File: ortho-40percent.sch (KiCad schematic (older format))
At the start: 7 parts

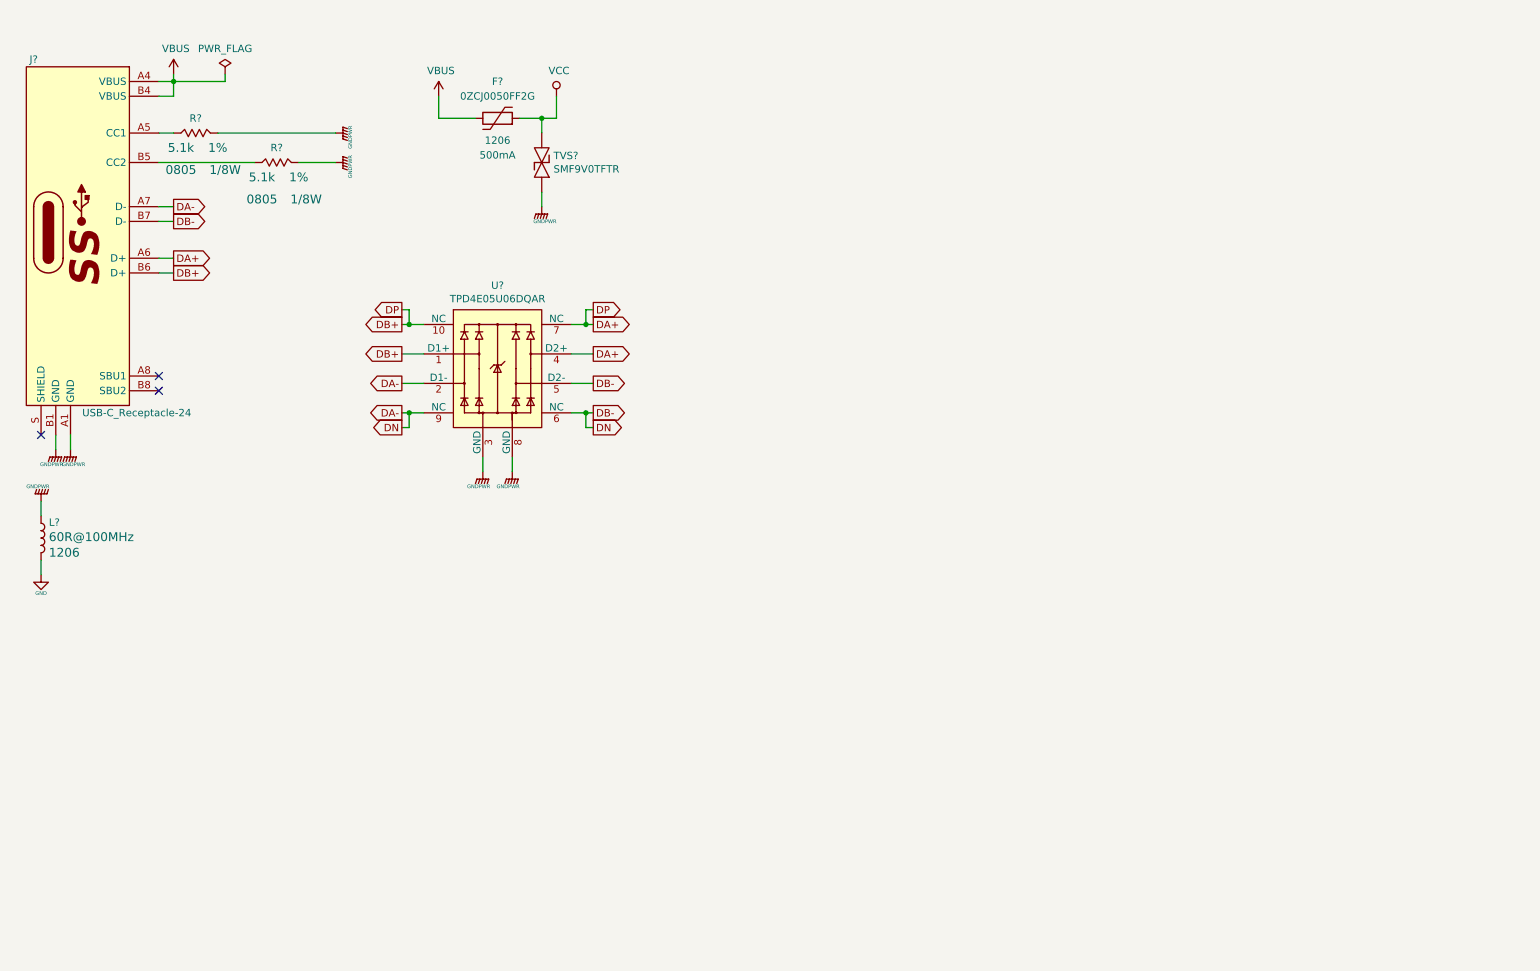
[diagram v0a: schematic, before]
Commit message: Created KeyMatrix schematic
Added new footprints and associated 3d models. Created KeyMatrix schematic sheet.
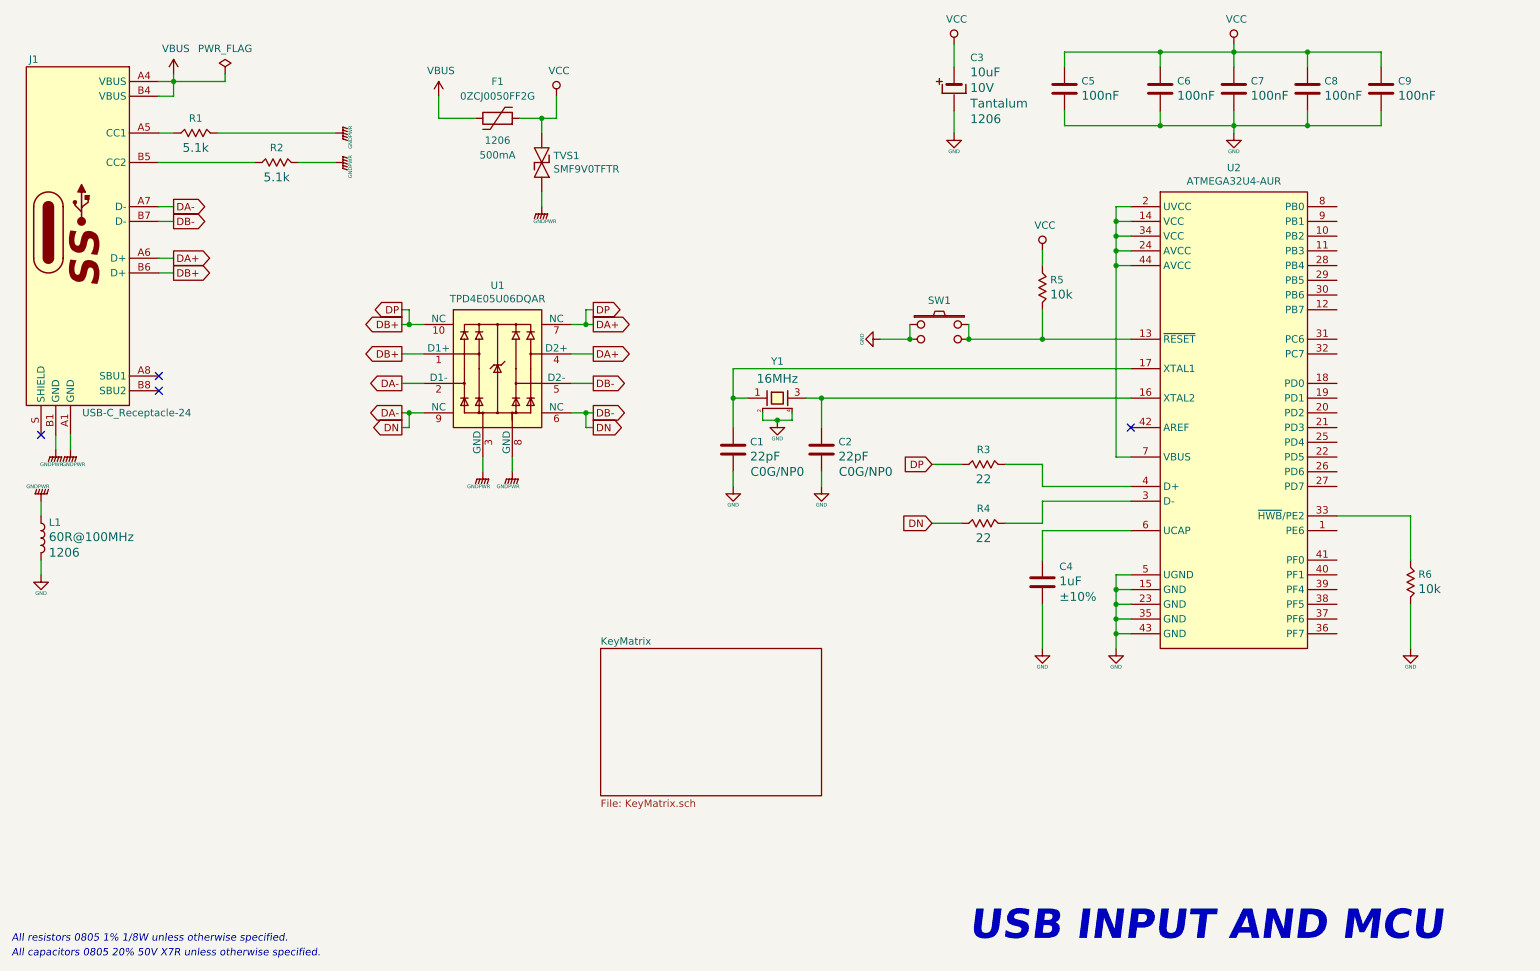
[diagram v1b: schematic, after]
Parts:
- added C1, C2, C4, C5, C6, C7, C8, C9: C, ortho-40percent:C_0805, symbol master-vampire_General:C
- added C3: CP_tantalum, ortho-40percent:CP_TANTALUM_1206, symbol master-vampire_General:CP_tantalum
- added R3, R4, R5, R6: R, ortho-40percent:R_0805, symbol master-vampire_General:R
- added SW1: SW_NO_4-Pin, ortho-40percent:SW_C+K_4-SMD-Gullwing_5.2x5.2mm_H1.6mm, symbol master-vampire_General:SW_NO_4-Pin
- added U2: U_ATmega32u4-AU, ortho-40percent:TQFP-44, symbol master-vampire_General:U_ATmega32u4-AU
- added Y1: XTAL_4Lead, ortho-40percent:XTAL_4-SMD_3.2x2.5mm, symbol master-vampire_General:XTAL_4Lead
- R1, R2: renamed from R?; footprint (none) -> ortho-40percent:R_0805
- TVS1: renamed from TVS?; footprint ortho-40percent:D_SOD-123F -> ortho-40percent:SOD-123F
- gave numbers to parts that had none: 4
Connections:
- net DA+: now also R3.2
- net DA-: now also R4.2
- net GND: now also C1.2, C2.2, C3.2, C4.2, C5.2, C6.2, C7.2, C8.2, C9.2, R6.1, SW1.1 (in), SW1.2 (in), U2.15 (GND), U2.23 (GND), U2.35 (GND), U2.43 (GND), U2.5 (UGND), Y1.2 (case), Y1.4 (case)
- net VCC: now also C3.1, C5.1, C6.1, C7.1, C8.1, C9.1, R5.2
- new net: C1.1, U2.17 (XTAL1), Y1.1
- new net: R5.1, SW1.3 (out), SW1.4 (out), U2.13 (~RESET)
- new net: U2.14 (VCC), U2.2 (UVCC), U2.24 (AVCC), U2.34 (VCC), U2.44 (AVCC), U2.7 (VBUS)
- new net: C2.1, U2.16 (XTAL2), Y1.3
- new net: R4.1, U2.3 (D-)
- new net: R6.2, U2.33 (~HWB~/PE2)
- new net: R3.1, U2.4 (D+)
- new net: C4.1, U2.6 (UCAP)
- no-connect marks 3 -> 4
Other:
- note added: "All capacitors 0805 20% 50V X7R unless otherwise specified."
- note added: "All resistors 0805 1% 1/8W unless otherwise specified."
- note added: "USB INPUT AND MCU"

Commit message: Case outline and mounting
Received kprepublic case, used dimensions to set drawing of case and pcb outline. Created M2 screw footprint and added mounting holes to project. Tied screws to power gnd, will possibly change to signal ground later. Changed switches to be kailh hotswaps.
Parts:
- added H1, H2, H3, H4, H5: H_MountingHole_Screw_withPin, ortho-40percent:H_Screw-M2_Countersunk, symbol master-vampire_General:H_MountingHole_Screw_withPin
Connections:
- net GNDPWR: now also H1.1, H2.1, H3.1, H4.1, H5.1
- net VCC: now also U2.14 (VCC), U2.2 (UVCC), U2.24 (AVCC), U2.34 (VCC), U2.44 (AVCC), U2.7 (VBUS)
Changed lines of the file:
@@
 F1 "KeyMatrix.sch" 50
 $EndSheet
+$Comp
+L power:VCC #PWR026
+U 1 1 604393E0
+P 8500 1850
+F 0 "#PWR026" H 8500 1700 50  0001 C CNN
+F 1 "VCC" H 8517 2023 50  0000 C CNN
+F 2 "" H 8500 1850 50  0001 C CNN
+F 3 "" H 8500 1850 50  0001 C CNN
+	1    8500 1850
+	1    0    0    -1
+$EndComp
+Wire Wire Line
+	8500 1850 8500 2000
+Connection ~ 8500 2000
+$Comp
+L master-vampire_General:H_MountingHole_Screw_withPin H1
+U 1 1 604407EC
+P 1500 5100
+F 0 "H1" V 1650 5050 50  0000 L CNN
+F 1 "H_MountingHole_Screw_withPin" H 1628 5055 50  0001 L CNN
+F 2 "ortho-40percent:H_Screw-M2_Countersunk" H 1500 5100 50  0001 C CNN
+F 3 "" H 1500 5100 50  0001 C CNN
+F 4 "DNP" H 1600 5300 50  0001 C CNN "MPN"
+F 5 "DNP" H 1700 5400 50  0001 C CNN "Manufacturer"
+F 6 "DNP" H 1800 5500 50  0001 C CNN "Supplier PN"
+F 7 "DNP" H 1900 5600 50  0001 C CNN "Supplier"
+F 8 "DNP" H 2000 5700 50  0001 C CNN "Package"
+	1    1500 5100
+	0    -1   -1   0
+$EndComp
+$Comp
+L master-vampire_General:H_MountingHole_Screw_withPin H2
+U 1 1 6041FFC7
+P 1750 5100
+F 0 "H2" V 1900 5050 50  0000 L CNN
+F 1 "H_MountingHole_Screw_withPin" H 1878 5055 50  0001 L CNN
+F 2 "ortho-40percent:H_Screw-M2_Countersunk" H 1750 5100 50  0001 C CNN
+F 3 "" H 1750 5100 50  0001 C CNN
+F 4 "DNP" H 1850 5300 50  0001 C CNN "MPN"
+F 5 "DNP" H 1950 5400 50  0001 C CNN "Manufacturer"
+F 6 "DNP" H 2050 5500 50  0001 C CNN "Supplier PN"
+F 7 "DNP" H 2150 5600 50  0001 C CNN "Supplier"
+F 8 "DNP" H 2250 5700 50  0001 C CNN "Package"
+	1    1750 5100
+	0    -1   -1   0
+$EndComp
+$Comp
+L master-vampire_General:H_MountingHole_Screw_withPin H3
+U 1 1 60420244
+P 2000 5100
+F 0 "H3" V 2150 5050 50  0000 L CNN
+F 1 "H_MountingHole_Screw_withPin" H 2128 5055 50  0001 L CNN
+F 2 "ortho-40percent:H_Screw-M2_Countersunk" H 2000 5100 50  0001 C CNN
+F 3 "" H 2000 5100 50  0001 C CNN
+F 4 "DNP" H 2100 5300 50  0001 C CNN "MPN"
+F 5 "DNP" H 2200 5400 50  0001 C CNN "Manufacturer"
+F 6 "DNP" H 2300 5500 50  0001 C CNN "Supplier PN"
+F 7 "DNP" H 2400 5600 50  0001 C CNN "Supplier"
+F 8 "DNP" H 2500 5700 50  0001 C CNN "Package"
+	1    2000 5100
+	0    -1   -1   0
+$EndComp
+$Comp
+L master-vampire_General:H_MountingHole_Screw_withPin H4
+U 1 1 60420819
+P 2250 5100
+F 0 "H4" V 2400 5050 50  0000 L CNN
+F 1 "H_MountingHole_Screw_withPin" H 2378 5055 50  0001 L CNN
+F 2 "ortho-40percent:H_Screw-M2_Countersunk" H 2250 5100 50  0001 C CNN
+F 3 "" H 2250 5100 50  0001 C CNN
+F 4 "DNP" H 2350 5300 50  0001 C CNN "MPN"
+F 5 "DNP" H 2450 5400 50  0001 C CNN "Manufacturer"
+F 6 "DNP" H 2550 5500 50  0001 C CNN "Supplier PN"
+F 7 "DNP" H 2650 5600 50  0001 C CNN "Supplier"
+F 8 "DNP" H 2750 5700 50  0001 C CNN "Package"
+	1    2250 5100
+	0    -1   -1   0
+$EndComp
+$Comp
+L power:GNDPWR #PWR025
+U 1 1 60421692
+P 1500 5500
+F 0 "#PWR025" H 1500 5300 50  0001 C CNN
+F 1 "GNDPWR" H 1550 5400 25  0000 R CNN
+F 2 "" H 1500 5450 50  0001 C CNN
+F 3 "" H 1500 5450 50  0001 C CNN
+	1    1500 5500
+	1    0    0    -1
+$EndComp
+Wire Wire Line
+	1500 5400 1500 5450
+Wire Wire Line
+	1750 5400 1750 5450
+Wire Wire Line
+	1750 5450 1500 5450
+Connection ~ 1500 5450
+Wire Wire Line
+	1500 5450 1500 5500
+Wire Wire Line
+	2000 5400 2000 5450
+Wire Wire Line
+	2000 5450 1750 5450
+Connection ~ 1750 5450
+Wire Wire Line
+	2250 5400 2250 5450
+Wire Wire Line
+	2250 5450 2000 5450
+Connection ~ 2000 5450
+$Comp
+L master-vampire_General:H_MountingHole_Screw_withPin H5
+U 1 1 6043642C
+P 2500 5100
+F 0 "H5" V 2650 5050 50  0000 L CNN
+F 1 "H_MountingHole_Screw_withPin" H 2628 5055 50  0001 L CNN
+F 2 "ortho-40percent:H_Screw-M2_Countersunk" H 2500 5100 50  0001 C CNN
+F 3 "" H 2500 5100 50  0001 C CNN
+F 4 "DNP" H 2600 5300 50  0001 C CNN "MPN"
+F 5 "DNP" H 2700 5400 50  0001 C CNN "Manufacturer"
+F 6 "DNP" H 2800 5500 50  0001 C CNN "Supplier PN"
+F 7 "DNP" H 2900 5600 50  0001 C CNN "Supplier"
+F 8 "DNP" H 3000 5700 50  0001 C CNN "Package"
+	1    2500 5100
+	0    -1   -1   0
+$EndComp
+Wire Wire Line
+	2500 5400 2500 5450
+Wire Wire Line
+	2500 5450 2250 5450
+Connection ~ 2250 5450
 $EndSCHEMATC

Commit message: ESD overhaul and mechanical finish
Finished mounting hole placement with respect to case dimensions. Rotated all switches 180 to allow for placement of USB-C connector. Redid ground connections to have connector shield grounded to case and signal ground grounded to case, but not connected on PCB. Added tab on PCB edge to allow USB-C connector to extend further out of case. Replaced 9V TVS with 6V TVS.
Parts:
- removed TVS1: TVS_Bidirectional, ortho-40percent:SOD-123F, symbol master-vampire_General:TVS_Bidirectional
- added TVS1: TVS_Unidirectional, ortho-40percent:SOD-123F, symbol master-vampire_General:TVS_Unidirectional
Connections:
- net GND: now also H1.1, H2.1, H3.1, H5.1, J1.A1 (GND), J1.B1 (GND), R1.1, R2.1, U1.3 (GND), U1.8 (GND), TVS1.A
- net GNDPWR: now also J1.S (SHIELD); no longer H1.1, H2.1, H3.1, H5.1, J1.A1 (GND), J1.B1 (GND), R1.1, R2.1, U1.3 (GND), U1.8 (GND)
- net VCC: now also TVS1.K
- no-connect marks 4 -> 3
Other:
- moved on the sheet: H4, L1

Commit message: 2u footprint and plate comments
Finished 2u footprint in all styles. Added cutouts by using Cmts.User layer.
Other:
- note added: "Star ground for micro connections"
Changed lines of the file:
@@
 	1    0    0    -1
 $EndComp
+Text Notes 6750 1750 0    50   ~ 0
+Star ground for micro connections
 $EndSCHEMATC

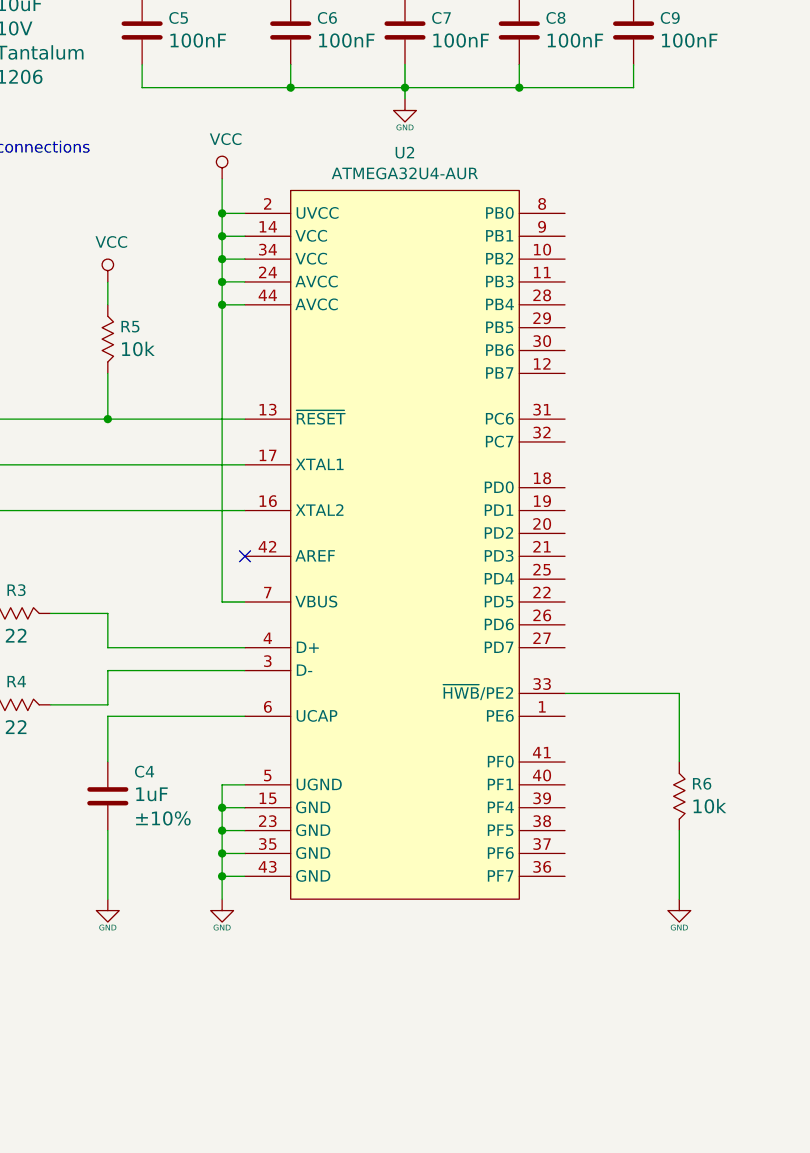
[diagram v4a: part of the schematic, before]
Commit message: Micro change and origin reset
Returned origin to center hole of bottom-left switch instead of pin 1 hole.
Added 3mm ground trace margin and mtg hole margin.
Created 44-VQFN footprint and schematic symbol, and updated micro to new part.
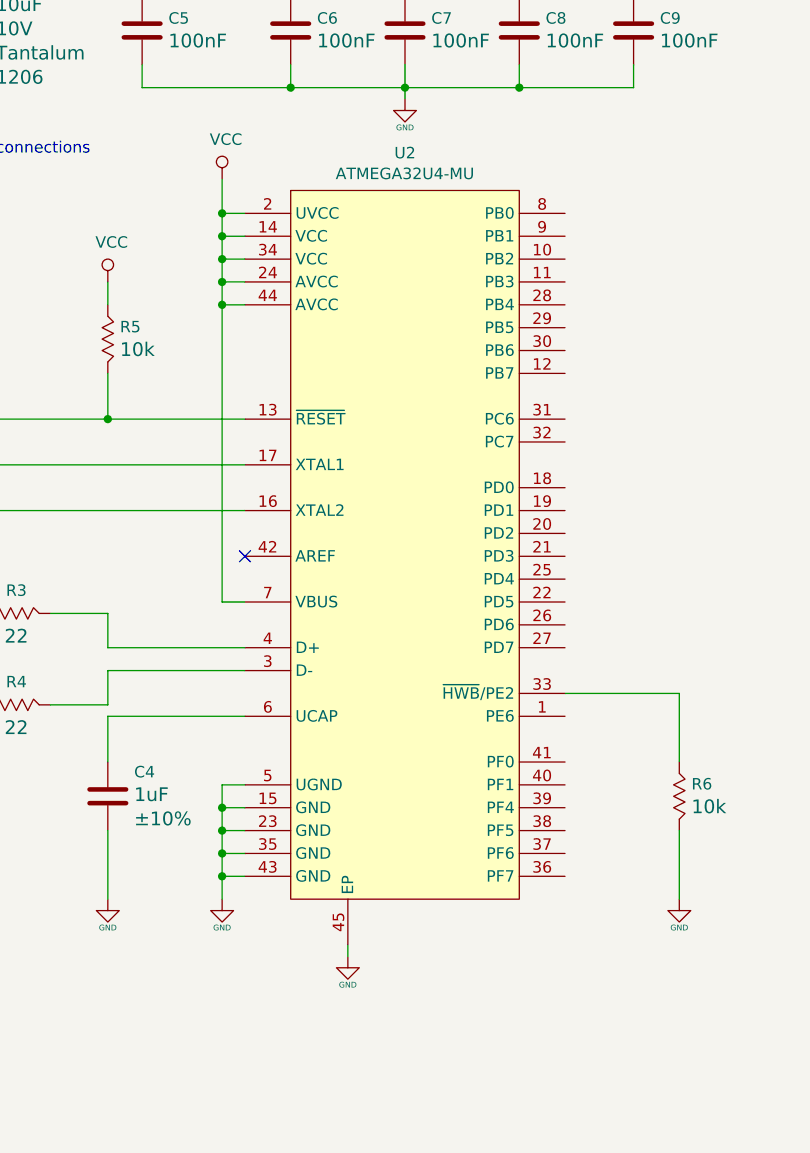
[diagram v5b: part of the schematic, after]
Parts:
- removed U2: U_ATmega32u4-AU, ortho-40percent:TQFP-44, symbol master-vampire_General:U_ATmega32u4-AU
- added U2: U_ATmega32u4-MU, ortho-40percent:VQFN-44-1EP_7x7mm_P0.5mm_ThermalVias, symbol master-vampire_General:U_ATmega32u4-MU
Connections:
- net GND: now also U2.15 (GND), U2.23 (GND), U2.35 (GND), U2.43 (GND), U2.45 (EP), U2.5 (UGND)
- net VCC: now also U2.14 (VCC), U2.2 (UVCC), U2.24 (AVCC), U2.34 (VCC), U2.44 (AVCC), U2.7 (VBUS)
- net at C1.1, Y1.1: now also U2.17 (XTAL1)
- net at R5.1, SW1.3 (out), SW1.4 (out): now also U2.13 (~RESET)
- net at C2.1, Y1.3: now also U2.16 (XTAL2)
- net at R4.1: now also U2.3 (D-)
- net at R6.2: now also U2.33 (~HWB~/PE2)
- net at R3.1: now also U2.4 (D+)
- net at C4.1: now also U2.6 (UCAP)
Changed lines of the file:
@@
 Wire Wire Line
 	5900 3100 8600 3100
-$Comp
-L master-vampire_General:U_ATmega32u4-AU U2
-U 1 1 5F24A76C
-P 9300 3500
-F 0 "U2" H 9300 5264 50  0000 C CNN
-F 1 "U_ATmega32u4-AU" H 9200 3400 50  0001 C CNN
-F 2 "ortho-40percent:TQFP-44" H 9200 3400 50  0001 C CNN
-F 3 "" H 9200 3400 50  0001 C CNN
-F 4 "Microchip Technology" H 9200 3400 50  0001 C CNN "Manufacturer"
-F 5 "ATMEGA32U4-AUR" H 9300 5173 50  0000 C CNN "MPN"
-F 6 "DigiKey" H 9200 3400 50  0001 C CNN "Supplier"
-F 7 "ATMEGA32U4-AURCT-ND" H 9200 3400 50  0001 C CNN "Supplier PN"
-F 8 "TQFP-44" H 9200 3400 50  0001 C CNN "Package"
-	1    9300 3500
-	1    0    0    -1
-$EndComp
 NoConn ~ 8600 3500
 Wire Wire Line
@@
 $EndComp
 $Comp
-L power:GND #PWR?
+L power:GND #PWR027
 U 1 1 60523F3F
 P 4600 1900
-F 0 "#PWR?" H 4600 1650 50  0001 C CNN
+F 0 "#PWR027" H 4600 1650 50  0001 C CNN
 F 1 "GND" H 4600 1775 25  0000 C CNN
 F 2 "" H 4600 1900 50  0001 C CNN
@@
 $EndComp
 $Comp
-L power:GND #PWR?
+L power:GND #PWR09
 U 1 1 60524B44
 P 3200 1500
-F 0 "#PWR?" H 3200 1250 50  0001 C CNN
+F 0 "#PWR09" H 3200 1250 50  0001 C CNN
 F 1 "GND" H 3200 1375 25  0000 C CNN
 F 2 "" H 3200 1500 50  0001 C CNN
@@
 $EndComp
 $Comp
-L power:GND #PWR?
+L power:GND #PWR010
 U 1 1 6052508C
 P 3200 1700
-F 0 "#PWR?" H 3200 1450 50  0001 C CNN
+F 0 "#PWR010" H 3200 1450 50  0001 C CNN
 F 1 "GND" H 3200 1575 25  0000 C CNN
 F 2 "" H 3200 1700 50  0001 C CNN
@@
 $EndComp
 $Comp
-L power:GND #PWR?
+L power:GND #PWR04
 U 1 1 605258D7
 P 1400 3650
-F 0 "#PWR?" H 1400 3400 50  0001 C CNN
+F 0 "#PWR04" H 1400 3400 50  0001 C CNN
 F 1 "GND" H 1400 3525 25  0000 C CNN
 F 2 "" H 1400 3650 50  0001 C CNN
@@
 $EndComp
 $Comp
-L power:GNDPWR #PWR?
+L power:GNDPWR #PWR03
 U 1 1 60525FA7
 P 1200 3650
-F 0 "#PWR?" H 1200 3450 50  0001 C CNN
+F 0 "#PWR03" H 1200 3450 50  0001 C CNN
 F 1 "GNDPWR" H 1275 3525 25  0000 R CNN
 F 2 "" H 1200 3600 50  0001 C CNN
@@
 	1400 3600 1400 3650
 $Comp
-L power:GNDPWR #PWR?
+L power:GNDPWR #PWR06
 U 1 1 60532468
 P 1500 4500
-F 0 "#PWR?" H 1500 4300 50  0001 C CNN
+F 0 "#PWR06" H 1500 4300 50  0001 C CNN
 F 1 "GNDPWR" H 1575 4375 25  0000 R CNN
 F 2 "" H 1500 4450 50  0001 C CNN
@@
 	1500 4500 1500 4400
 $Comp
-L power:GND #PWR?
+L power:GND #PWR025
 U 1 1 60537DDD
 P 4400 3800
-F 0 "#PWR?" H 4400 3550 50  0001 C CNN
+F 0 "#PWR025" H 4400 3550 50  0001 C CNN
 F 1 "GND" H 4400 3675 25  0000 C CNN
 F 2 "" H 4400 3800 50  0001 C CNN
@@
 $EndComp
 $Comp
-L power:GND #PWR?
+L power:GND #PWR011
 U 1 1 605382B2
 P 4200 3800
-F 0 "#PWR?" H 4200 3550 50  0001 C CNN
+F 0 "#PWR011" H 4200 3550 50  0001 C CNN
 F 1 "GND" H 4200 3675 25  0000 C CNN
 F 2 "" H 4200 3800 50  0001 C CNN
@@
 $EndComp
 $Comp
-L power:GND #PWR?
+L power:GND #PWR07
 U 1 1 60538D51
 P 1500 5500
-F 0 "#PWR?" H 1500 5250 50  0001 C CNN
+F 0 "#PWR07" H 1500 5250 50  0001 C CNN
 F 1 "GND" H 1500 5375 25  0000 C CNN
 F 2 "" H 1500 5500 50  0001 C CNN
@@
 Text Notes 6750 1750 0    50   ~ 0
 Star ground for micro connections
+$Comp
+L master-vampire_General:U_ATmega32u4-MU U2
+U 1 1 607C806A
+P 9300 3500
+F 0 "U2" H 9300 5264 50  0000 C CNN
+F 1 "U_ATmega32u4-MU" H 9200 3400 50  0001 C CNN
+F 2 "ortho-40percent:VQFN-44-1EP_7x7mm_P0.5mm_ThermalVias" H 9200 3400 50  0001 C CNN
+F 3 "" H 9200 3400 50  0001 C CNN
+F 4 "Microchip Technology" H 9200 3400 50  0001 C CNN "Manufacturer"
+F 5 "ATMEGA32U4-MU" H 9300 5173 50  0000 C CNN "MPN"
+F 6 "DigiKey" H 9200 3400 50  0001 C CNN "Supplier"
+F 7 "ATMEGA32U4-MU-ND" H 9200 3400 50  0001 C CNN "Supplier PN"
+F 8 "VQFN-44-1EP" H 9200 3400 50  0001 C CNN "Package"
+	1    9300 3500
+	1    0    0    -1
+$EndComp
+$Comp
+L power:GND #PWR028
+U 1 1 607CA4F0
+P 9050 5250
+F 0 "#PWR028" H 9050 5000 50  0001 C CNN
+F 1 "GND" H 9050 5125 25  0000 C CNN
+F 2 "" H 9050 5250 50  0001 C CNN
+F 3 "" H 9050 5250 50  0001 C CNN
+	1    9050 5250
+	1    0    0    -1
+$EndComp
+Wire Wire Line
+	9050 5250 9050 5200
 $EndSCHEMATC
